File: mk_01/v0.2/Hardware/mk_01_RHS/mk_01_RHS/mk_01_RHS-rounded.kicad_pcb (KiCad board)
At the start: 2 copper layers, 184.1 x 102.9 mm, 90 parts, among them SW1 SW_Push_Dual, U1 nice_nano

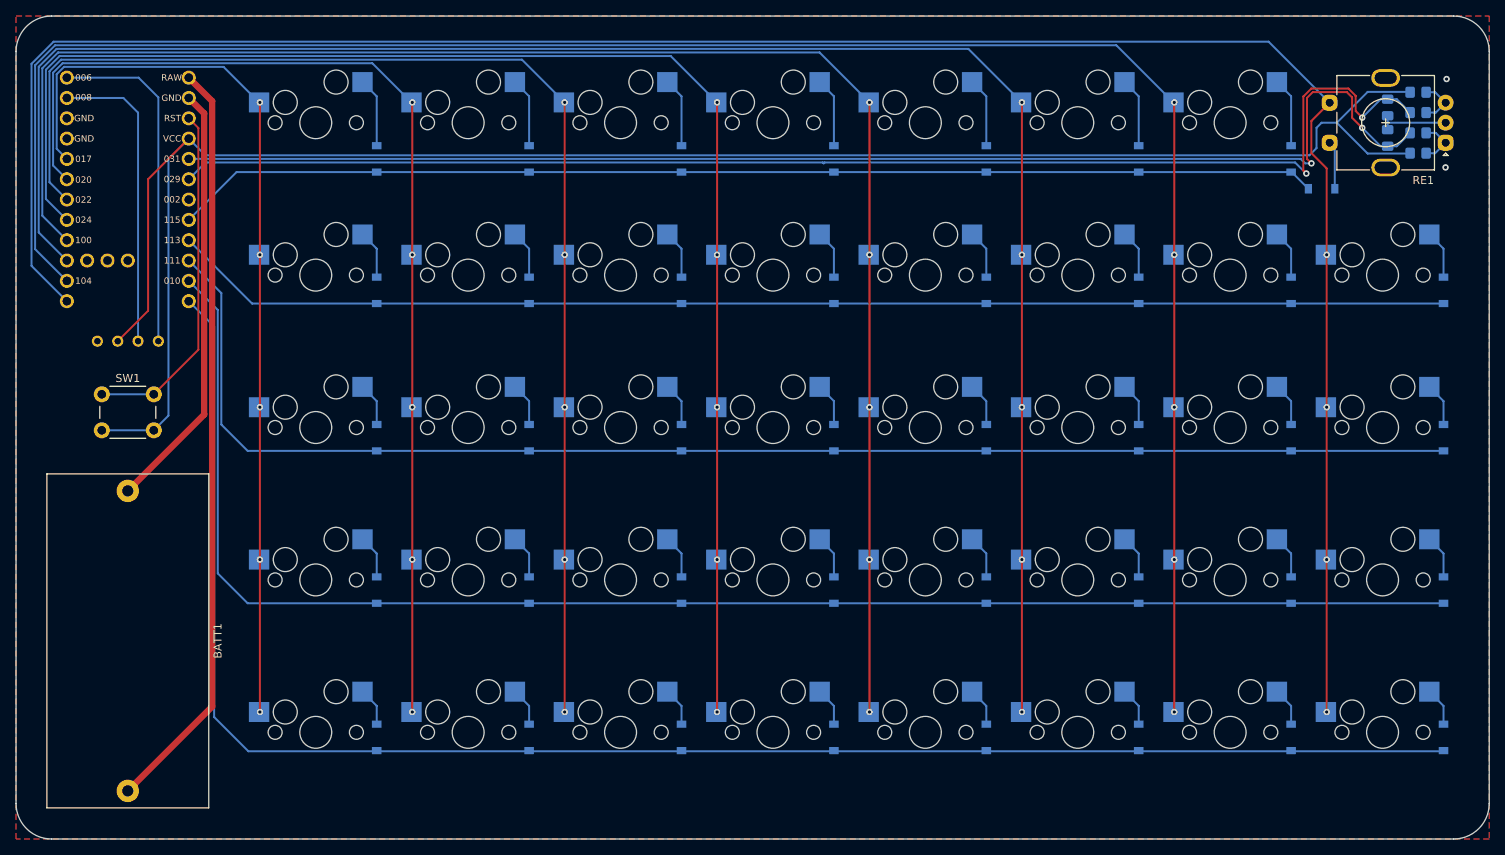
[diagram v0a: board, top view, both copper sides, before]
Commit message: Right hand side mostly completed
The right hand side of the keyboard is pretty much complete, and after a final checkover of everything I think it's ready for production. I'm going to clean up the left hand side board design and schematic to match the right hand schematic style, since I based the left hand side on v0.1, and the right hand side was done from scratch.
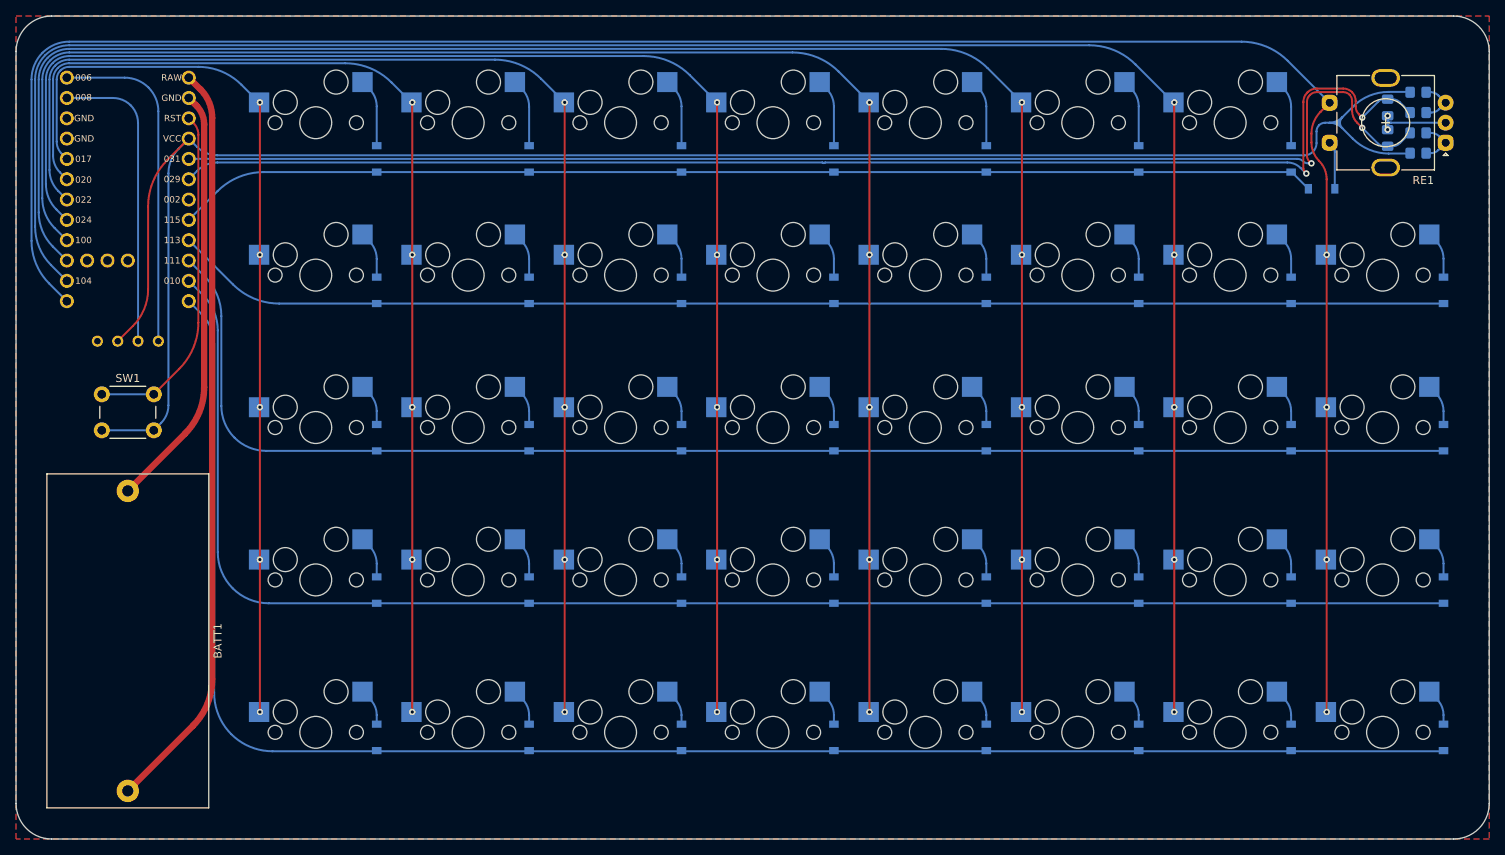
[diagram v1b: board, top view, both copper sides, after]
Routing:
- net col7: track 276.0 -> 274.3 mm
- net col6: track 251.1 -> 250.0 mm
- net col5: track 228.4 -> 227.4 mm
- net row4: track 208.8 -> 207.8 mm
- net col4: track 205.7 -> 204.8 mm
- net row3: track 192.8 -> 191.9 mm
- net Earth: track 8.98 -> 9.88 mm
- net col3: track 183.1 -> 182.2 mm
- net row2: track 176.3 -> 175.4 mm
- net Net-(U1-Pad19): track 169.0 -> 168.2 mm
- net col2: track 160.3 -> 159.5 mm
- net col1: track 137.5 -> 136.8 mm
- net Net-(BATT1-Pad2): track 94.7 -> 94.1 mm
- net col0: track 114.8 -> 114.2 mm
- net RE_B: track 167.2 -> 166.6 mm
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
